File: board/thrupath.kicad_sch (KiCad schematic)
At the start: 114 parts, among them J6 BEL_FUSE_0826-1G1T-23-F, J7 BEL_FUSE_0826-1G1T-23-F, U4 XC7S15-1FTGB196C, U5 KSZ9031RN, U6 KSZ9031RN, U7 ECS-2016MVQ-250-CN-TR, U8 ECS-2016MVQ-250-CN-TR

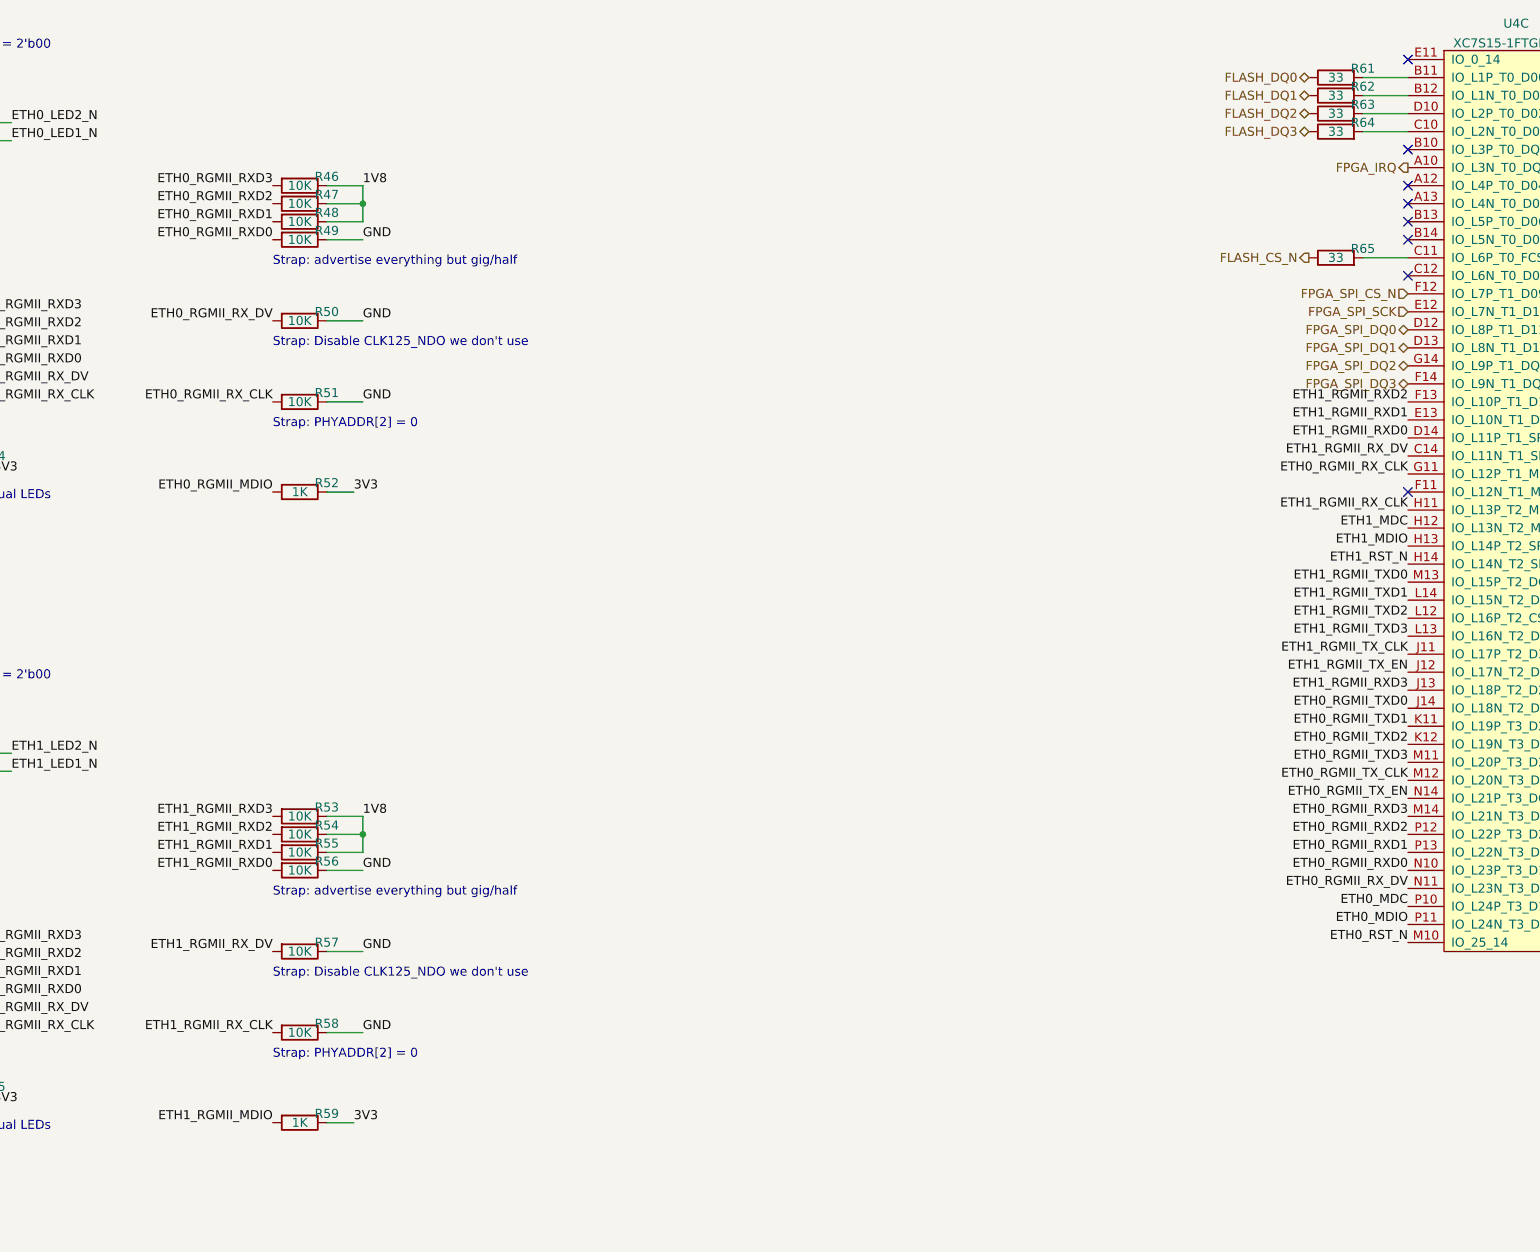
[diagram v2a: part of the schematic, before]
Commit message: Continued initial layout. First PHY fully routed including connection to FPGA. Hooked up 0402 bypass caps under FPGA. Flash is roughly placed.
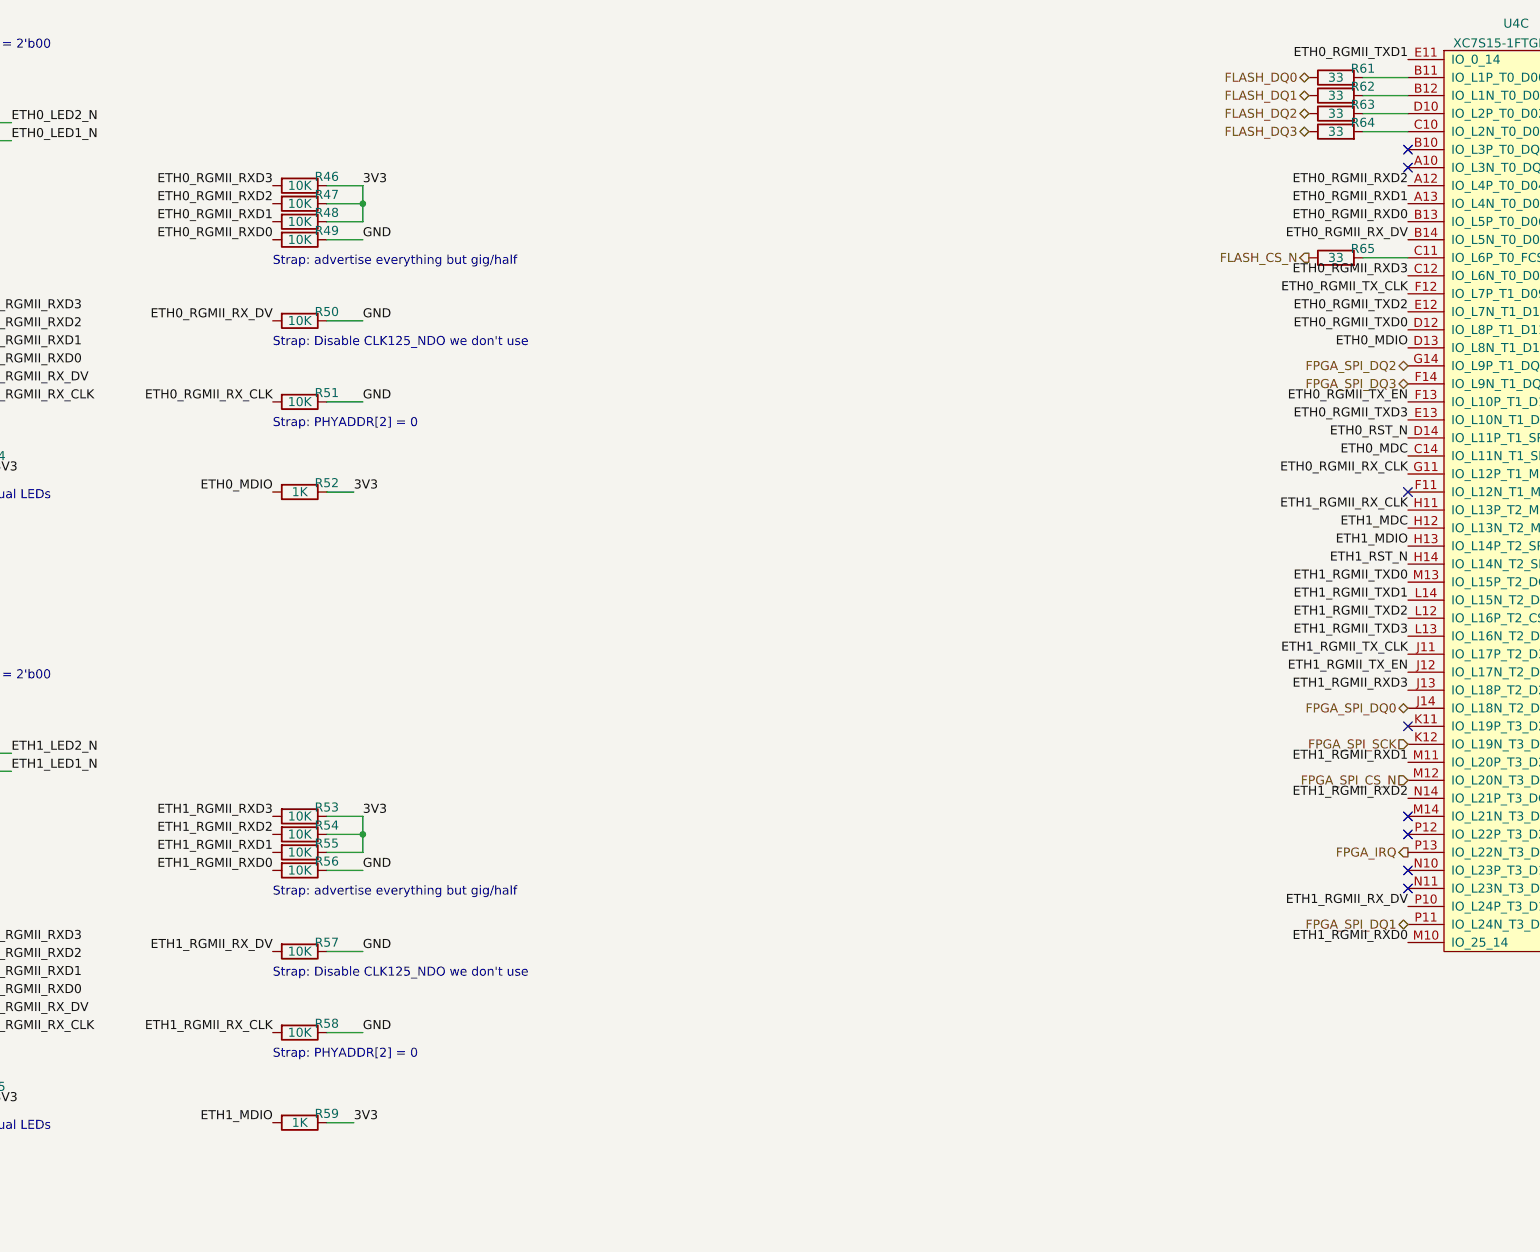
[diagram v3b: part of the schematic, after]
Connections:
- net 1V8 is gone; now on net 3V3: R46.1, R47.1, R48.1, R53.1, R54.1, R55.1
- net ETH0_RGMII_MDIO is gone; now on net ETH0_MDIO: R52.2
- net ETH1_RGMII_MDIO is gone; now on net ETH1_MDIO: R59.2
- net ETH0_MDC: now also U4.C14 (IO_L11N_T1_SRCC_14); no longer U4.P10 (IO_L24P_T3_D17_14)
- net ETH0_MDIO: now also U4.D13 (IO_L8N_T1_D12_14); no longer U4.P11 (IO_L24N_T3_D16_14)
- net ETH0_RGMII_RXD0: now also U4.B13 (IO_L5P_T0_D06_14); no longer U4.N10 (IO_L23P_T3_D19_14)
- net ETH0_RGMII_RXD1: now also U4.A13 (IO_L4N_T0_D05_14); no longer U4.P13 (IO_L22N_T3_D20_14)
- net ETH0_RGMII_RXD2: now also U4.A12 (IO_L4P_T0_D04_14); no longer U4.P12 (IO_L22P_T3_D21_14)
- net ETH0_RGMII_RXD3: now also U4.C12 (IO_L6N_T0_D08_VREF_14); no longer U4.M14 (IO_L21N_T3_DQS_D22_14)
- net ETH0_RGMII_RX_DV: now also U4.B14 (IO_L5N_T0_D07_14); no longer U4.N11 (IO_L23N_T3_D18_14)
- net ETH0_RGMII_TXD0: now also U4.D12 (IO_L8P_T1_D11_14); no longer U4.J14 (IO_L18N_T2_D27_14)
- net ETH0_RGMII_TXD1: now also U4.E11 (IO_0_14); no longer U4.K11 (IO_L19P_T3_D26_14)
- net ETH0_RGMII_TXD2: now also U4.E12 (IO_L7N_T1_D10_14); no longer U4.K12 (IO_L19N_T3_D25_VREF_14)
- net ETH0_RGMII_TXD3: now also U4.E13 (IO_L10N_T1_D15_14); no longer U4.M11 (IO_L20P_T3_D24_14)
- net ETH0_RGMII_TX_CLK: now also U4.F12 (IO_L7P_T1_D09_14); no longer U4.M12 (IO_L20N_T3_D23_14)
- net ETH0_RGMII_TX_EN: now also U4.F13 (IO_L10P_T1_D14_14); no longer U4.N14 (IO_L21P_T3_DQS_14)
- net ETH0_RST_N: now also U4.D14 (IO_L11P_T1_SRCC_14); no longer U4.M10 (IO_25_14)
- net ETH1_RGMII_RXD0: now also U4.M10 (IO_25_14); no longer U4.D14 (IO_L11P_T1_SRCC_14)
- net ETH1_RGMII_RXD1: now also U4.M11 (IO_L20P_T3_D24_14); no longer U4.E13 (IO_L10N_T1_D15_14)
- net ETH1_RGMII_RXD2: now also U4.N14 (IO_L21P_T3_DQS_14); no longer U4.F13 (IO_L10P_T1_D14_14)
- net ETH1_RGMII_RX_DV: now also U4.P10 (IO_L24P_T3_D17_14); no longer U4.C14 (IO_L11N_T1_SRCC_14)
- net FPGA_IRQ: now also U4.P13 (IO_L22N_T3_D20_14); no longer U4.A10 (IO_L3N_T0_DQS_EMCCLK_14)
- net FPGA_SPI_CS_N: now also U4.M12 (IO_L20N_T3_D23_14); no longer U4.F12 (IO_L7P_T1_D09_14)
- net FPGA_SPI_DQ0: now also U4.J14 (IO_L18N_T2_D27_14); no longer U4.D12 (IO_L8P_T1_D11_14)
- net FPGA_SPI_DQ1: now also U4.P11 (IO_L24N_T3_D16_14); no longer U4.D13 (IO_L8N_T1_D12_14)
- net FPGA_SPI_SCK: now also U4.K12 (IO_L19N_T3_D25_VREF_14); no longer U4.E12 (IO_L7N_T1_D10_14)
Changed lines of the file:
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@@
   (title_block
     (title "Active 10/100/1000baseT Tap")
-    (date "2022-12-20")
+    (date "2022-12-21")
     (rev "0.1")
     (company "Antikernel Labs")
@@
   (no_connect (at 143.51 165.1))
   (no_connect (at 143.51 176.53))
+  (no_connect (at 364.49 134.62))
   (no_connect (at 143.51 87.63))
-  (no_connect (at 364.49 20.32))
+  (no_connect (at 364.49 35.56))
+  (no_connect (at 364.49 127))
+  (no_connect (at 364.49 129.54))
+  (no_connect (at 364.49 114.3))
+  (no_connect (at 364.49 137.16))
   (no_connect (at 364.49 81.28))
   (no_connect (at 86.36 157.48))
-  (no_connect (at 364.49 38.1))
-  (no_connect (at 364.49 40.64))
-  (no_connect (at 364.49 43.18))
-  (no_connect (at 364.49 45.72))
   (no_connect (at 364.49 33.02))
-  (no_connect (at 364.49 50.8))
   (no_connect (at 143.51 76.2))
   (no_connect (at 86.36 68.58))
@@
     (effects (font (size 1.27 1.27)) (justify right bottom))
   )
-  (label "ETH0_RGMII_RXD0" (at 364.49 134.62 180)
-    (effects (font (size 1.27 1.27)) (justify right bottom))
-  )
-  (label "1V8" (at 217.17 38.1 0)
+  (label "ETH0_RGMII_RXD0" (at 364.49 43.18 180)
+    (effects (font (size 1.27 1.27)) (justify right bottom))
+  )
+  (label "3V3" (at 217.17 38.1 0)
     (effects (font (size 1.27 1.27)) (justify left bottom))
   )
@@
     (effects (font (size 1.27 1.27)) (justify right bottom))
   )
-  (label "ETH0_RGMII_TXD3" (at 364.49 119.38 180)
+  (label "ETH0_RGMII_TXD3" (at 364.49 71.12 180)
     (effects (font (size 1.27 1.27)) (justify right bottom))
   )
@@
     (effects (font (size 1.27 1.27)) (justify left bottom))
   )
-  (label "1V8" (at 217.17 127 0)
+  (label "3V3" (at 217.17 127 0)
     (effects (font (size 1.27 1.27)) (justify left bottom))
   )
@@
     (effects (font (size 1.27 1.27)) (justify right bottom))
   )
-  (label "ETH0_RGMII_TXD0" (at 364.49 111.76 180)
+  (label "ETH0_RGMII_TXD0" (at 364.49 58.42 180)
     (effects (font (size 1.27 1.27)) (justify right bottom))
   )
@@
     (effects (font (size 1.27 1.27)) (justify left bottom))
   )
-  (label "ETH0_RST_N" (at 364.49 144.78 180)
-    (effects (font (size 1.27 1.27)) (justify right bottom))
-  )
-  (label "ETH1_RGMII_RXD2" (at 364.49 68.58 180)
+  (label "ETH0_RST_N" (at 364.49 73.66 180)
+    (effects (font (size 1.27 1.27)) (justify right bottom))
+  )
+  (label "ETH1_RGMII_RXD2" (at 364.49 124.46 180)
     (effects (font (size 1.27 1.27)) (justify right bottom))
   )
@@
     (effects (font (size 1.27 1.27)) (justify right bottom))
   )
-  (label "ETH0_RGMII_TX_EN" (at 364.49 124.46 180)
+  (label "ETH0_RGMII_TX_EN" (at 364.49 68.58 180)
     (effects (font (size 1.27 1.27)) (justify right bottom))
   )
@@
     (effects (font (size 1.27 1.27)) (justify right bottom))
   )
-  (label "ETH0_RGMII_RX_DV" (at 364.49 137.16 180)
+  (label "ETH0_RGMII_RX_DV" (at 364.49 45.72 180)
     (effects (font (size 1.27 1.27)) (justify right bottom))
   )
@@
     (effects (font (size 1.27 1.27)) (justify left bottom))
   )
-  (label "ETH0_RGMII_MDIO" (at 204.47 81.28 180)
+  (label "ETH0_MDIO" (at 204.47 81.28 180)
     (effects (font (size 1.27 1.27)) (justify right bottom))
   )
@@
     (effects (font (size 1.27 1.27)) (justify left bottom))
   )
-  (label "ETH0_MDC" (at 364.49 139.7 180)
+  (label "ETH0_MDC" (at 364.49 76.2 180)
     (effects (font (size 1.27 1.27)) (justify right bottom))
   )
@@
     (effects (font (size 1.27 1.27)) (justify right bottom))
   )
-  (label "ETH0_RGMII_RXD1" (at 364.49 132.08 180)
+  (label "ETH0_RGMII_RXD1" (at 364.49 40.64 180)
     (effects (font (size 1.27 1.27)) (justify right bottom))
   )
@@
     (effects (font (size 1.27 1.27)) (justify left bottom))
   )
-  (label "ETH1_RGMII_MDIO" (at 204.47 170.18 180)
-    (effects (font (size 1.27 1.27)) (justify right bottom))
-  )
-  (label "ETH0_RGMII_TX_CLK" (at 364.49 121.92 180)
-    (effects (font (size 1.27 1.27)) (justify right bottom))
-  )
-  (label "ETH1_RGMII_RX_DV" (at 364.49 76.2 180)
+  (label "ETH1_MDIO" (at 204.47 170.18 180)
+    (effects (font (size 1.27 1.27)) (justify right bottom))
+  )
+  (label "ETH0_RGMII_TX_CLK" (at 364.49 53.34 180)
+    (effects (font (size 1.27 1.27)) (justify right bottom))
+  )
+  (label "ETH1_RGMII_RX_DV" (at 364.49 139.7 180)
     (effects (font (size 1.27 1.27)) (justify right bottom))
   )
@@
     (effects (font (size 1.27 1.27)) (justify right bottom))
   )
-  (label "ETH1_RGMII_RXD1" (at 364.49 71.12 180)
+  (label "ETH1_RGMII_RXD1" (at 364.49 119.38 180)
     (effects (font (size 1.27 1.27)) (justify right bottom))
   )
@@
     (effects (font (size 1.27 1.27)) (justify left bottom))
   )
-  (label "ETH0_RGMII_TXD2" (at 364.49 116.84 180)
-    (effects (font (size 1.27 1.27)) (justify right bottom))
-  )
-  (label "ETH0_RGMII_TXD1" (at 364.49 114.3 180)
+  (label "ETH0_RGMII_TXD2" (at 364.49 55.88 180)
+    (effects (font (size 1.27 1.27)) (justify right bottom))
+  )
+  (label "ETH0_RGMII_TXD1" (at 364.49 20.32 180)
     (effects (font (size 1.27 1.27)) (justify right bottom))
   )
@@
     (effects (font (size 1.27 1.27)) (justify left bottom))
   )
-  (label "ETH0_MDIO" (at 364.49 142.24 180)
+  (label "ETH0_MDIO" (at 364.49 60.96 180)
     (effects (font (size 1.27 1.27)) (justify right bottom))
   )
@@
     (effects (font (size 1.27 1.27)) (justify right bottom))
   )
-  (label "ETH0_RGMII_RXD3" (at 364.49 127 180)
+  (label "ETH0_RGMII_RXD3" (at 364.49 50.8 180)
     (effects (font (size 1.27 1.27)) (justify right bottom))
   )
@@
     (effects (font (size 1.27 1.27)) (justify left bottom))
   )
-  (label "ETH0_RGMII_RXD2" (at 364.49 129.54 180)
-    (effects (font (size 1.27 1.27)) (justify right bottom))
-  )
-  (label "ETH1_RGMII_RXD0" (at 364.49 73.66 180)
+  (label "ETH0_RGMII_RXD2" (at 364.49 38.1 180)
+    (effects (font (size 1.27 1.27)) (justify right bottom))
+  )
+  (label "ETH1_RGMII_RXD0" (at 364.49 144.78 180)
     (effects (font (size 1.27 1.27)) (justify right bottom))
   )
@@
     (effects (font (size 1.27 1.27)) (justify right))
   )
-  (hierarchical_label "FPGA_SPI_CS_N" (shape input) (at 364.49 53.34 180)
+  (hierarchical_label "FPGA_SPI_CS_N" (shape input) (at 364.49 121.92 180)
     (effects (font (size 1.27 1.27)) (justify right))
   )
@@
     (effects (font (size 1.27 1.27)) (justify right))
   )
-  (hierarchical_label "FPGA_SPI_SCK" (shape input) (at 364.49 55.88 180)
+  (hierarchical_label "FPGA_SPI_SCK" (shape input) (at 364.49 116.84 180)
     (effects (font (size 1.27 1.27)) (justify right))
   )
-  (hierarchical_label "FPGA_IRQ" (shape output) (at 364.49 35.56 180)
+  (hierarchical_label "FPGA_IRQ" (shape output) (at 364.49 132.08 180)
     (effects (font (size 1.27 1.27)) (justify right))
   )
@@
     (effects (font (size 1.27 1.27)) (justify right))
   )
-  (hierarchical_label "FPGA_SPI_DQ1" (shape bidirectional) (at 364.49 60.96 180)
+  (hierarchical_label "FPGA_SPI_DQ1" (shape bidirectional) (at 364.49 142.24 180)
     (effects (font (size 1.27 1.27)) (justify right))
   )
-  (hierarchical_label "FPGA_SPI_DQ0" (shape bidirectional) (at 364.49 58.42 180)
+  (hierarchical_label "FPGA_SPI_DQ0" (shape bidirectional) (at 364.49 111.76 180)
     (effects (font (size 1.27 1.27)) (justify right))
   )
